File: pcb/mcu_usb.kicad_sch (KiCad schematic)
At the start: 33 parts, among them J12 USB_C_Receptacle, J13 UPDI, U10 CP2102N-A02-GQFN24, U11 TLV75533PDBV, U9 AVR128DA48-E/PT, Y1 32.768kHz

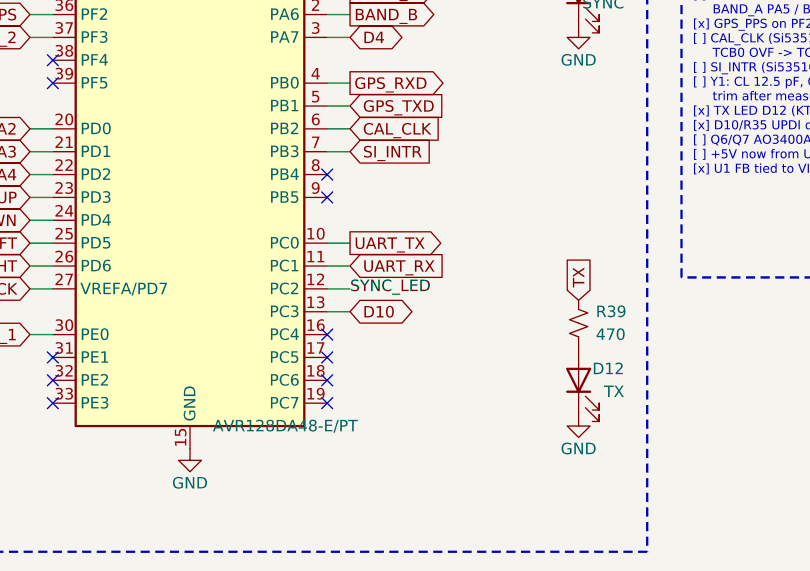
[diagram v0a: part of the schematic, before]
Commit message: UI: 128x32 I2C OLED -> 1.3in SH1106 SPI 7-pin DS1 (as Si5351AVFO, DNP) on SPI1 ALT1 PC4/PC6 + CS PC7, DC PB4, RES PB5; FB1+C25-C27 rail filter; VFO 10k/10k/100n RC on all 7 buttons (R50-R63); D-pad stays PD3-PD6; layout note; regen PDF
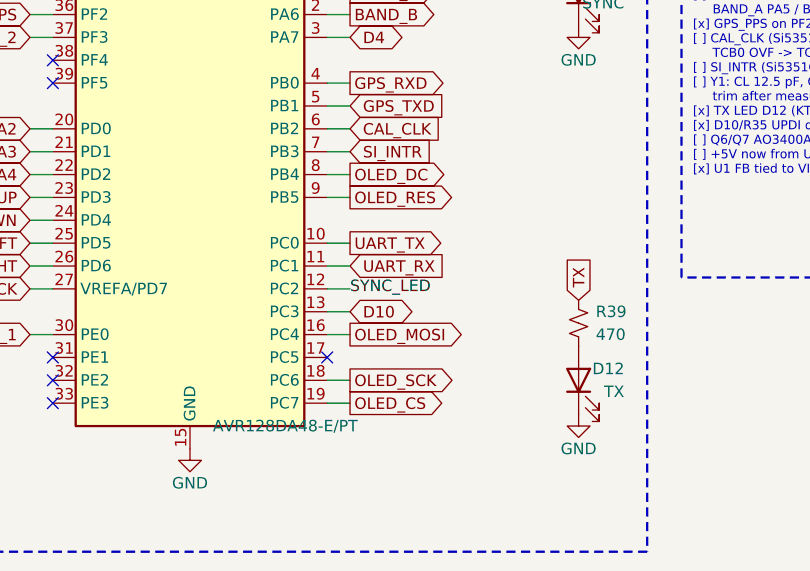
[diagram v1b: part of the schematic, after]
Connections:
- net OLED_MOSI: now reaches U9.16 (PC4)
- net OLED_SCK: now reaches U9.18 (PC6)
- net OLED_CS: now reaches U9.19 (PC7)
- net OLED_DC: now reaches U9.8 (PB4)
- net OLED_RES: now reaches U9.9 (PB5)
- no-connect marks 27 -> 22
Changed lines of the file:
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@@
-	)
-	(no_connect
-		(at 111.76 153.67)
-	)
-	(no_connect
-		(at 111.76 156.21)
-	)
-	(no_connect
-		(at 111.76 171.45)
 	)
 	(no_connect
 		(at 111.76 173.99)
-	)
-	(no_connect
-		(at 111.76 176.53)
-	)
-	(no_connect
-		(at 111.76 179.07)
 	)
 	(no_connect
@@
 		)
 	)
+	(wire
+		(pts
+			(xy 111.76 171.45)
+			(xy 114.3 171.45)
+		)
+		(stroke
+			(width 0)
+			(type default)
+		)
+	)
+	(global_label "OLED_MOSI"
+		(shape output)
+		(at 114.3 171.45 0)
+		(fields_autoplaced yes)
+		(effects
+			(font
+				(size 1.27 1.27)
+				(color 130 0 130 1)
+			)
+			(justify left)
+		)
+		(property "Intersheetrefs" "${INTERSHEET_REFS}"
+			(at 114.3 171.45 0)
+			(effects
+				(font
+					(size 1.27 1.27)
+				)
+				(hide yes)
+			)
+		)
+	)
+	(wire
+		(pts
+			(xy 111.76 176.53)
+			(xy 114.3 176.53)
+		)
+		(stroke
+			(width 0)
+			(type default)
+		)
+	)
+	(global_label "OLED_SCK"
+		(shape output)
+		(at 114.3 176.53 0)
+		(fields_autoplaced yes)
+		(effects
+			(font
+				(size 1.27 1.27)
+				(color 130 0 130 1)
+			)
+			(justify left)
+		)
+		(property "Intersheetrefs" "${INTERSHEET_REFS}"
+			(at 114.3 176.53 0)
+			(effects
+				(font
+					(size 1.27 1.27)
+				)
+				(hide yes)
+			)
+		)
+	)
+	(wire
+		(pts
+			(xy 111.76 179.07)
+			(xy 114.3 179.07)
+		)
+		(stroke
+			(width 0)
+			(type default)
+		)
+	)
+	(global_label "OLED_CS"
+		(shape output)
+		(at 114.3 179.07 0)
+		(fields_autoplaced yes)
+		(effects
+			(font
+				(size 1.27 1.27)
+				(color 130 0 130 1)
+			)
+			(justify left)
+		)
+		(property "Intersheetrefs" "${INTERSHEET_REFS}"
+			(at 114.3 179.07 0)
+			(effects
+				(font
+					(size 1.27 1.27)
+				)
+				(hide yes)
+			)
+		)
+	)
+	(wire
+		(pts
+			(xy 111.76 153.67)
+			(xy 114.3 153.67)
+		)
+		(stroke
+			(width 0)
+			(type default)
+		)
+	)
+	(global_label "OLED_DC"
+		(shape output)
+		(at 114.3 153.67 0)
+		(fields_autoplaced yes)
+		(effects
+			(font
+				(size 1.27 1.27)
+				(color 130 0 130 1)
+			)
+			(justify left)
+		)
+		(property "Intersheetrefs" "${INTERSHEET_REFS}"
+			(at 114.3 153.67 0)
+			(effects
+				(font
+					(size 1.27 1.27)
+				)
+				(hide yes)
+			)
+		)
+	)
+	(wire
+		(pts
+			(xy 111.76 156.21)
+			(xy 114.3 156.21)
+		)
+		(stroke
+			(width 0)
+			(type default)
+		)
+	)
+	(global_label "OLED_RES"
+		(shape output)
+		(at 114.3 156.21 0)
+		(fields_autoplaced yes)
+		(effects
+			(font
+				(size 1.27 1.27)
+				(color 130 0 130 1)
+			)
+			(justify left)
+		)
+		(property "Intersheetrefs" "${INTERSHEET_REFS}"
+			(at 114.3 156.21 0)
+			(effects
+				(font
+					(size 1.27 1.27)
+				)
+				(hide yes)
+			)
+		)
+	)

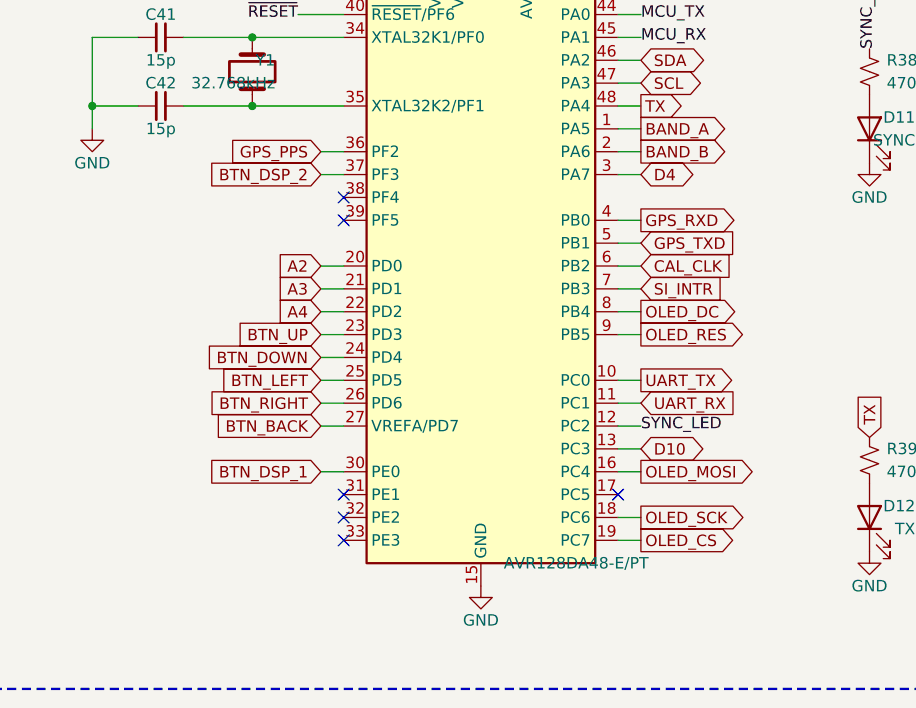
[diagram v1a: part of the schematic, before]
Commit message: IO: Option B spare GPIO - J4 1x10 (D7/PA7, D17/PC3, D19/PC5, D38/A20/PF4, D39/A21/PF5, GND between), J5 1x12 (D22-D24/A0-A2/PD0-PD2, D31-D33/A9-A11/PE1-PE3, GND between); DxCore 48pin-standard net names; NC flags removed from PC5/PE1-3/PF4/PF5; J8/J10 shifted left; regen PDF
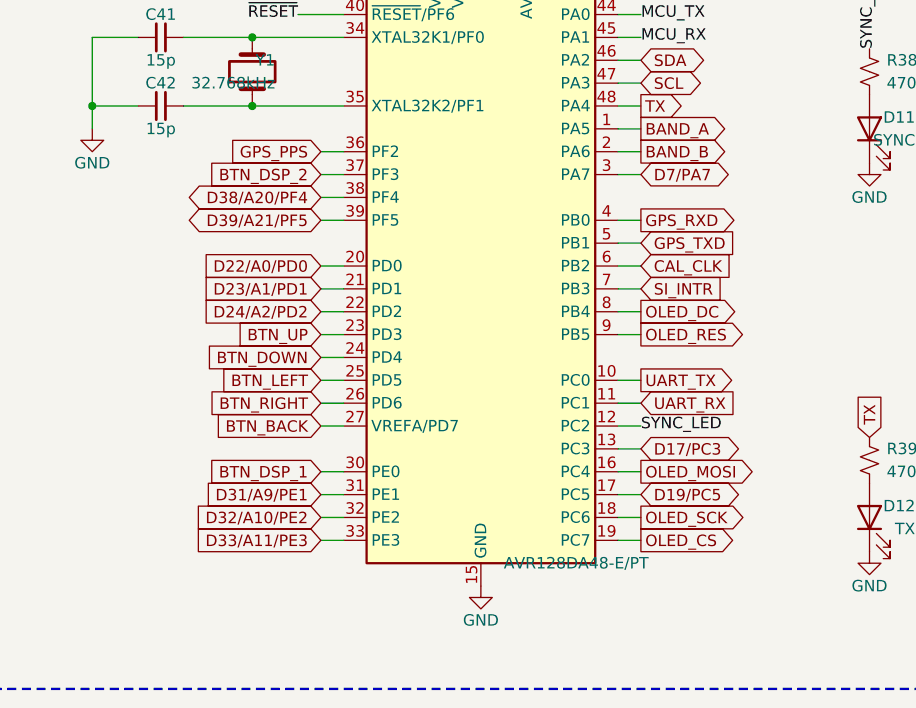
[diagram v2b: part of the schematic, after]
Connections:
- net D19/PC5: now reaches U9.17 (PC5)
- net D31/A9/PE1: now reaches U9.31 (PE1)
- net D32/A10/PE2: now reaches U9.32 (PE2)
- net D33/A11/PE3: now reaches U9.33 (PE3)
- net D38/A20/PF4: now reaches U9.38 (PF4)
- net D39/A21/PF5: now reaches U9.39 (PF5)
- net A2 renamed D22/A0/PD0
- net A3 renamed D23/A1/PD1
- net A4 renamed D24/A2/PD2
- net D10 renamed D17/PC3
- net D4 renamed D7/PA7
- no-connect marks 22 -> 16
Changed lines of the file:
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@@
 		)
-	)
-	(no_connect
-		(at 111.76 173.99)
-	)
-	(no_connect
-		(at 81.28 140.97)
-	)
-	(no_connect
-		(at 81.28 143.51)
-	)
-	(no_connect
-		(at 81.28 173.99)
-	)
-	(no_connect
-		(at 81.28 176.53)
-	)
-	(no_connect
-		(at 81.28 179.07)
 	)
 	(wire
@@
 		)
 	)
-	(global_label "D4"
+	(global_label "D7/PA7"
 		(shape bidirectional)
 		(at 114.3 138.43 0)
@@
 		)
 	)
-	(global_label "D10"
+	(global_label "D17/PC3"
 		(shape bidirectional)
 		(at 114.3 168.91 0)
@@
 		)
 	)
-	(global_label "A2"
+	(global_label "D22/A0/PD0"
 		(shape input)
 		(at 78.74 148.59 180)
@@
 		)
 	)
-	(global_label "A3"
+	(global_label "D23/A1/PD1"
 		(shape input)
 		(at 78.74 151.13 180)
@@
 		)
 	)
-	(global_label "A4"
+	(global_label "D24/A2/PD2"
 		(shape input)
 		(at 78.74 153.67 180)
@@
 			(effects
 				(font
+					(size 1.27 1.27)
+				)
+				(hide yes)
+			)
+		)
+	)
+	(wire
+		(pts
+			(xy 111.76 173.99) (xy 114.3 173.99)
+		)
+		(stroke
+			(width 0)
+			(type default)
+		)
+	)
+	(global_label "D19/PC5"
+		(shape bidirectional)
+		(at 114.3 173.99 0)
+		(fields_autoplaced yes)
+		(effects
+			(font
+				(size 1.27 1.27)
+				(color 0 0 0 1)
+			)
+			(justify left)
+		)
+		(property "Intersheetrefs" "${INTERSHEET_REFS}"
+			(at 114.3 173.99 0)
+			(effects
+				(font
+					(size 1.27 1.27)
+				)
+				(hide yes)
+			)
+		)
+	)
+	(wire
+		(pts
+			(xy 81.28 140.97) (xy 78.74 140.97)
+		)
+		(stroke
+			(width 0)
+			(type default)
+		)
+	)
+	(global_label "D38/A20/PF4"
+		(shape bidirectional)
+		(at 78.74 140.97 180)
+		(fields_autoplaced yes)
+		(effects
+			(font
+				(size 1.27 1.27)
+				(color 0 0 0 1)
+			)
+			(justify right)
+		)
+		(property "Intersheetrefs" "${INTERSHEET_REFS}"
+			(at 78.74 140.97 0)
+			(effects
+				(font
+					(size 1.27 1.27)
+				)
+				(hide yes)
+			)
+		)
+	)
+	(wire
+		(pts
+			(xy 81.28 143.51) (xy 78.74 143.51)
+		)
+		(stroke
+			(width 0)
+			(type default)
+		)
+	)
+	(global_label "D39/A21/PF5"
+		(shape bidirectional)
+		(at 78.74 143.51 180)
+		(fields_autoplaced yes)
+		(effects
+			(font
+				(size 1.27 1.27)
+				(color 0 0 0 1)
+			)
+			(justify right)
+		)
+		(property "Intersheetrefs" "${INTERSHEET_REFS}"
+			(at 78.74 143.51 0)
+			(effects
+				(font
+					(size 1.27 1.27)
+				)
+				(hide yes)
+			)
+		)
+	)
+	(wire
+		(pts
+			(xy 81.28 173.99) (xy 78.74 173.99)
+		)
+		(stroke
+			(width 0)
+			(type default)
+		)
+	)
+	(global_label "D31/A9/PE1"
+		(shape input)
+		(at 78.74 173.99 180)
+		(fields_autoplaced yes)
+		(effects
+			(font
+				(size 1.27 1.27)
+				(color 0 0 0 1)
+			)
+			(justify right)
+		)
+		(property "Intersheetrefs" "${INTERSHEET_REFS}"
+			(at 78.74 173.99 0)
+			(effects
+				(font
+					(size 1.27 1.27)
+				)
+				(hide yes)
+			)
+		)
+	)
+	(wire
+		(pts
+			(xy 81.28 176.53) (xy 78.74 176.53)
+		)
+		(stroke
+			(width 0)
+			(type default)
+		)
+	)
+	(global_label "D32/A10/PE2"
+		(shape input)
+		(at 78.74 176.53 180)
+		(fields_autoplaced yes)
+		(effects
+			(font
+				(size 1.27 1.27)
+				(color 0 0 0 1)
+			)
+			(justify right)
+		)
+		(property "Intersheetrefs" "${INTERSHEET_REFS}"
+			(at 78.74 176.53 0)
+			(effects
+				(font
+					(size 1.27 1.27)
+				)
+				(hide yes)
+			)
+		)
+	)
+	(wire
+		(pts
+			(xy 81.28 179.07) (xy 78.74 179.07)
+		)
+		(stroke
+			(width 0)
+			(type default)
+		)
+	)
+	(global_label "D33/A11/PE3"
+		(shape input)
+		(at 78.74 179.07 180)
+		(fields_autoplaced yes)
+		(effects
+			(font
+				(size 1.27 1.27)
+				(color 0 0 0 1)
+			)
+			(justify right)
+		)
+		(property "Intersheetrefs" "${INTERSHEET_REFS}"
+			(at 78.74 179.07 0)
+			(effects
+				(font

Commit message: IO: header GPIO net labels slash -> underscore (D7_PA7, D22_A0_PD0, ...); renames only; regen PDF
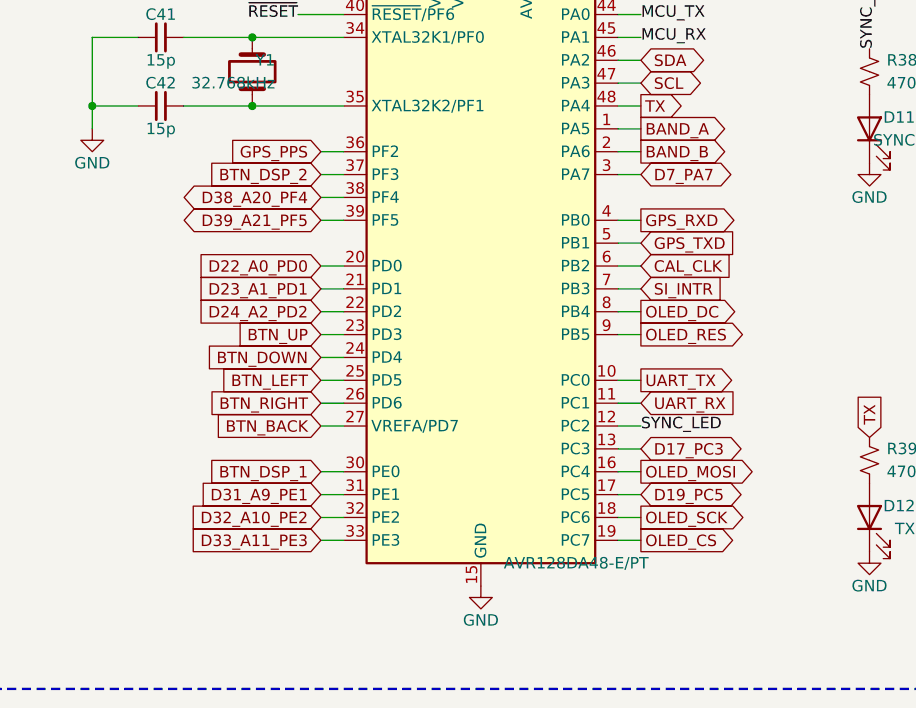
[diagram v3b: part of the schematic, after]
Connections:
- net D17/PC3 renamed D17_PC3
- net D19/PC5 renamed D19_PC5
- net D22/A0/PD0 renamed D22_A0_PD0
- net D23/A1/PD1 renamed D23_A1_PD1
- net D24/A2/PD2 renamed D24_A2_PD2
- net D31/A9/PE1 renamed D31_A9_PE1
- net D32/A10/PE2 renamed D32_A10_PE2
- net D33/A11/PE3 renamed D33_A11_PE3
- net D38/A20/PF4 renamed D38_A20_PF4
- net D39/A21/PF5 renamed D39_A21_PF5
- net D7/PA7 renamed D7_PA7
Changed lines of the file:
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@@
 		)
 	)
-	(global_label "D7/PA7"
+	(global_label "D7_PA7"
 		(shape bidirectional)
 		(at 114.3 138.43 0)
@@
 		)
 	)
-	(global_label "D17/PC3"
+	(global_label "D17_PC3"
 		(shape bidirectional)
 		(at 114.3 168.91 0)
@@
 		)
 	)
-	(global_label "D22/A0/PD0"
+	(global_label "D22_A0_PD0"
 		(shape input)
 		(at 78.74 148.59 180)
@@
 		)
 	)
-	(global_label "D23/A1/PD1"
+	(global_label "D23_A1_PD1"
 		(shape input)
 		(at 78.74 151.13 180)
@@
 		)
 	)
-	(global_label "D24/A2/PD2"
+	(global_label "D24_A2_PD2"
 		(shape input)
 		(at 78.74 153.67 180)
@@
 		)
 	)
-	(global_label "D19/PC5"
+	(global_label "D19_PC5"
 		(shape bidirectional)
 		(at 114.3 173.99 0)
@@
 		)
 	)
-	(global_label "D38/A20/PF4"
+	(global_label "D38_A20_PF4"
 		(shape bidirectional)
 		(at 78.74 140.97 180)
@@
 		)
 	)
-	(global_label "D39/A21/PF5"
+	(global_label "D39_A21_PF5"
 		(shape bidirectional)
 		(at 78.74 143.51 180)
@@
 		)
 	)
-	(global_label "D31/A9/PE1"
+	(global_label "D31_A9_PE1"
 		(shape input)
 		(at 78.74 173.99 180)
@@
 		)
 	)
-	(global_label "D32/A10/PE2"
+	(global_label "D32_A10_PE2"
 		(shape input)
 		(at 78.74 176.53 180)
@@
 		)
 	)
-	(global_label "D33/A11/PE3"
+	(global_label "D33_A11_PE3"
 		(shape input)
 		(at 78.74 179.07 180)
